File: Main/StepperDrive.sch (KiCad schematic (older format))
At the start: 4 parts, among them P2 RIGHT_STEPPER, P3 LEFT_STEPPER, U4 74HC595, U5 ULN2803A

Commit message: initial version of v3.0
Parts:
- U4: footprint (none) -> SMD_Packages:SO-16-N
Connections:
- net GND: now also U4.13 (G)
- net SR_LATCH: now also U4.12 (RCLK); no longer U4.13 (G)
- net +3V3: now reaches U4.10 (SRCLR)
- no-connect marks 3 -> 1
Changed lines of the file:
@@
 EESchema Schematic File Version 2
-LIBS:Mirobot-rescue
 LIBS:power
 LIBS:device
@@
 LIBS:memory
 LIBS:xilinx
-LIBS:microcontrollers
-LIBS:dsp
-LIBS:microchip
-LIBS:analog_switches
-LIBS:motorola
-LIBS:texas
-LIBS:intel
-LIBS:audio
-LIBS:interface
-LIBS:digital-audio
-LIBS:philips
-LIBS:display
-LIBS:cypress
-LIBS:siliconi
-LIBS:opto
-LIBS:atmel
-LIBS:contrib
-LIBS:valves
 LIBS:mirobot
 LIBS:Mirobot-cache
@@
 $EndComp
 $Comp
-L GND #PWR15
+L GND #PWR015
 U 1 1 56A00C21
 P 5600 4425
-F 0 "#PWR15" H 5600 4175 60  0001 C CNN
+F 0 "#PWR015" H 5600 4175 60  0001 C CNN
 F 1 "GND" H 5600 4275 60  0000 C CNN
 F 2 "" H 5600 4425 60  0000 C CNN
@@
 $EndComp
 $Comp
-L VSS #PWR16
+L VSS #PWR016
 U 1 1 56A00C27
 P 7275 4475
-F 0 "#PWR16" H 7275 4325 60  0001 C CNN
+F 0 "#PWR016" H 7275 4325 60  0001 C CNN
 F 1 "VSS" H 7275 4625 60  0000 C CNN
 F 2 "" H 7275 4475 60  0000 C CNN
@@
 F 0 "U4" H 4650 4325 50  0000 C CNN
 F 1 "74HC595" H 4500 3125 50  0000 C CNN
-F 2 "" H 4500 3725 50  0000 C CNN
+F 2 "SMD_Packages:SO-16-N" H 4500 3725 50  0001 C CNN
 F 3 "" H 4500 3725 50  0000 C CNN
 	1    4500 3725
 	1    0    0    -1
 $EndComp
-NoConn ~ 3675 3575
-NoConn ~ 3675 3775
 NoConn ~ 5325 4175
 Wire Wire Line
@@
 	3800 3475 3525 3475
 Wire Wire Line
-	3800 3575 3675 3575
-Wire Wire Line
-	3800 3775 3675 3775
+	2875 3575 3800 3575
+Wire Wire Line
+	3800 3775 3525 3775
 Wire Wire Line
 	5200 4175 5325 4175
@@
 Text HLabel 3525 3475 0    60   Input ~ 0
 SR_CLK
-Text HLabel 3525 3875 0    60   Input ~ 0
+Text HLabel 3525 3775 0    60   Input ~ 0
 SR_LATCH
+Wire Wire Line
+	2875 3575 2875 3100
+$Comp
+L +3V3 #PWR?
+U 1 1 56AB51FA
+P 2875 3100
+F 0 "#PWR?" H 2875 2950 60  0001 C CNN
+F 1 "+3V3" H 2875 3240 60  0000 C CNN
+F 2 "" H 2875 3100 60  0000 C CNN
+F 3 "" H 2875 3100 60  0000 C CNN
+	1    2875 3100
+	1    0    0    -1
+$EndComp
+Wire Wire Line
+	3525 3875 3525 4425
+$Comp
+L GND #PWR?
+U 1 1 56AB52F9
+P 3525 4425
+F 0 "#PWR?" H 3525 4175 60  0001 C CNN
+F 1 "GND" H 3525 4275 60  0000 C CNN
+F 2 "" H 3525 4425 60  0000 C CNN
+F 3 "" H 3525 4425 60  0000 C CNN
+	1    3525 4425
+	1    0    0    -1
+$EndComp
 $EndSCHEMATC

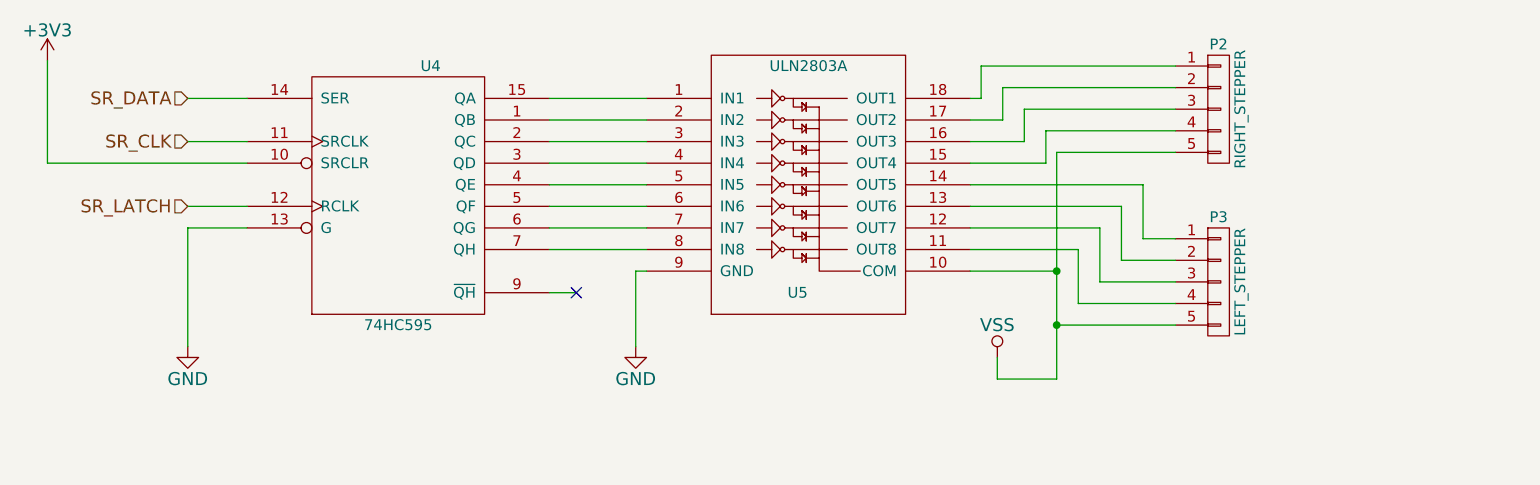
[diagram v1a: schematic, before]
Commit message: Update the BoM to embed it into KiCad
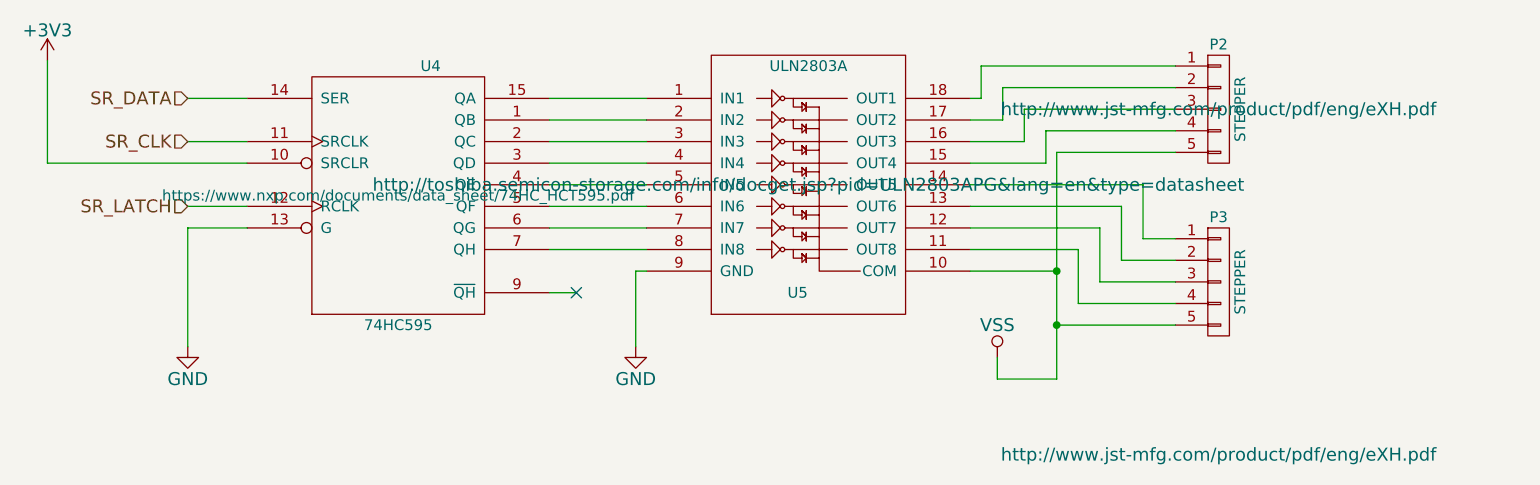
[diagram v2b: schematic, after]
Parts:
- P2: value RIGHT_STEPPER -> STEPPER; footprint Mirobot:JST_XH-1x05 -> Custom:JST_XH-1x05; Description (none) -> JST XH 5 Pin Socket Male; Manfr. Part Number (MFP) (none) -> B5B-XH-A; Manufacturer Name (MFN) (none) -> JST; Required (none) -> y; Source1 (none) -> http://www.digikey.co.uk/product-detail/en/B5B-XH-A(LF)(SN)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
- P3: value LEFT_STEPPER -> STEPPER; footprint Mirobot:JST_XH-1x05 -> Custom:JST_XH-1x05; Description (none) -> JST XH 5 Pin Socket Male; Manfr. Part Number (MFP) (none) -> B5B-XH-A; Manufacturer Name (MFN) (none) -> JST; Required (none) -> y; Source1 (none) -> http://www.digikey.co.uk/product-detail/en/B5B-XH-A(LF)(SN)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
- U4: Description (none) -> 8-Bit Serial Shift Register; Manfr. Part Number (MFP) (none) -> 74HC595D; Manufacturer Name (MFN) (none) -> NXP; Package ID (none) -> SO16; Required (none) -> y; Source2 (none) -> http://www.aliexpress.com/item/Hot-spot-200pcs-74HC595D-74H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
- U5: footprint Mirobot:SO-18 -> Custom:SO-18; Description (none) -> 8 Channel Darlington Sink Driver; Manfr. Part Number (MFP) (none) -> ULN2803AFWG; Manufacturer Name (MFN) (none) -> Toshiba; Package ID (none) -> SOP18; Required (none) -> y; Source2 (none) -> http://www.aliexpress.com/item/100-PCS-ULN2803AG-SOP-18-ULN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
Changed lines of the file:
@@
 LIBS:memory
 LIBS:xilinx
-LIBS:mirobot
+LIBS:custom-symbols
 LIBS:Mirobot-cache
 EELAYER 25 0
@@
 F 0 "U5" H 6350 3175 50  0000 C CNN
 F 1 "ULN2803A" H 6400 4225 50  0000 C CNN
-F 2 "Mirobot:SO-18" H 6400 3675 60  0001 C CNN
-F 3 "" H 6400 3675 60  0000 C CNN
+F 2 "Custom:SO-18" H 6400 3675 60  0001 C CNN
+F 3 "http://toshiba.semicon-storage.com/info/docget.jsp?pid=ULN2803APG&lang=en&type=datasheet" H 6400 3675 60  0000 C CNN
+F 4 "8 Channel Darlington Sink Driver" H 6400 3675 60  0001 C CNN "Description"
+F 5 "SOP18" H 6400 3675 60  0001 C CNN "Package ID"
+F 6 "Toshiba" H 6400 3675 60  0001 C CNN "Manufacturer Name (MFN)"
+F 7 "ULN2803AFWG" H 6400 3675 60  0001 C CNN "Manfr. Part Number (MFP)"
+F 8 "http://www.aliexpress.com/item/100-PCS-ULN2803AG-SOP-18-ULN2803-8ch-Darlington-Sink-Driver/32355854614.html" H 6400 3675 60  0001 C CNN "Source2"
+F 9 "y" H 6400 3675 60  0001 C CNN "Required"
 	1    6400 3675
 	1    0    0    -1
@@
 P 8300 3325
 F 0 "P2" H 8300 3625 50  0000 C CNN
-F 1 "RIGHT_STEPPER" V 8400 3325 50  0000 C CNN
-F 2 "Mirobot:JST_XH-1x05" H 8300 3325 60  0001 C CNN
-F 3 "" H 8300 3325 60  0000 C CNN
+F 1 "STEPPER" V 8400 3325 50  0000 C CNN
+F 2 "Custom:JST_XH-1x05" H 8300 3325 60  0001 C CNN
+F 3 "http://www.jst-mfg.com/product/pdf/eng/eXH.pdf" H 8300 3325 60  0000 C CNN
+F 4 "JST XH 5 Pin Socket Male" H 8300 3325 60  0001 C CNN "Description"
+F 5 "JST" H 8300 3325 60  0001 C CNN "Manufacturer Name (MFN)"
+F 6 "B5B-XH-A" H 8300 3325 60  0001 C CNN "Manfr. Part Number (MFP)"
+F 7 "http://www.digikey.co.uk/product-detail/en/B5B-XH-A(LF)(SN)/455-2270-ND/1530483" H 8300 3325 60  0001 C CNN "Source1"
+F 8 "y" H 8300 3325 60  0001 C CNN "Required"
 	1    8300 3325
 	1    0    0    -1
@@
 P 8300 4125
 F 0 "P3" H 8300 4425 50  0000 C CNN
-F 1 "LEFT_STEPPER" V 8400 4125 50  0000 C CNN
-F 2 "Mirobot:JST_XH-1x05" H 8300 4125 60  0001 C CNN
-F 3 "" H 8300 4125 60  0000 C CNN
+F 1 "STEPPER" V 8400 4125 50  0000 C CNN
+F 2 "Custom:JST_XH-1x05" H 8300 4125 60  0001 C CNN
+F 3 "http://www.jst-mfg.com/product/pdf/eng/eXH.pdf" H 8300 3325 60  0000 C CNN
+F 4 "JST XH 5 Pin Socket Male" H 8300 3325 60  0001 C CNN "Description"
+F 5 "JST" H 8300 3325 60  0001 C CNN "Manufacturer Name (MFN)"
+F 6 "B5B-XH-A" H 8300 3325 60  0001 C CNN "Manfr. Part Number (MFP)"
+F 7 "http://www.digikey.co.uk/product-detail/en/B5B-XH-A(LF)(SN)/455-2270-ND/1530483" H 8300 3325 60  0001 C CNN "Source1"
+F 8 "y" H 8300 3325 60  0001 C CNN "Required"
 	1    8300 4125
 	1    0    0    -1
 $EndComp
 $Comp
-L GND #PWR015
+L GND #PWR018
 U 1 1 56A00C21
 P 5600 4425
-F 0 "#PWR015" H 5600 4175 60  0001 C CNN
+F 0 "#PWR018" H 5600 4175 60  0001 C CNN
 F 1 "GND" H 5600 4275 60  0000 C CNN
 F 2 "" H 5600 4425 60  0000 C CNN
@@
 $EndComp
 $Comp
-L VSS #PWR016
+L VSS #PWR019
 U 1 1 56A00C27
 P 7275 4475
-F 0 "#PWR016" H 7275 4325 60  0001 C CNN
+F 0 "#PWR019" H 7275 4325 60  0001 C CNN
 F 1 "VSS" H 7275 4625 60  0000 C CNN
 F 2 "" H 7275 4475 60  0000 C CNN
@@
 F 1 "74HC595" H 4500 3125 50  0000 C CNN
 F 2 "SMD_Packages:SO-16-N" H 4500 3725 50  0001 C CNN
-F 3 "" H 4500 3725 50  0000 C CNN
+F 3 "https://www.nxp.com/documents/data_sheet/74HC_HCT595.pdf" H 4500 3725 50  0000 C CNN
+F 4 "8-Bit Serial Shift Register" H 4500 3725 60  0001 C CNN "Description"
+F 5 "SO16" H 4500 3725 60  0001 C CNN "Package ID"
+F 6 "NXP" H 4500 3725 60  0001 C CNN "Manufacturer Name (MFN)"
+F 7 "74HC595D" H 4500 3725 60  0001 C CNN "Manfr. Part Number (MFP)"
+F 8 "http://www.aliexpress.com/item/Hot-spot-200pcs-74HC595D-74HC595-SOP16-in-stock/32604602607.html" H 4500 3725 60  0001 C CNN "Source2"
+F 9 "y" H 4500 3725 60  0001 C CNN "Required"
 	1    4500 3725
 	1    0    0    -1
@@
 	2875 3575 2875 3100
 $Comp
-L +3V3 #PWR?
+L +3V3 #PWR020
 U 1 1 56AB51FA
 P 2875 3100
-F 0 "#PWR?" H 2875 2950 60  0001 C CNN
+F 0 "#PWR020" H 2875 2950 60  0001 C CNN
 F 1 "+3V3" H 2875 3240 60  0000 C CNN
 F 2 "" H 2875 3100 60  0000 C CNN
@@
 	3525 3875 3525 4425
 $Comp
-L GND #PWR?
+L GND #PWR021
 U 1 1 56AB52F9
 P 3525 4425
-F 0 "#PWR?" H 3525 4175 60  0001 C CNN
+F 0 "#PWR021" H 3525 4175 60  0001 C CNN
 F 1 "GND" H 3525 4275 60  0000 C CNN
 F 2 "" H 3525 4425 60  0000 C CNN
